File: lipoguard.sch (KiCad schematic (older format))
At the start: 13 parts, among them P1 CONN_2, P2 CONN_2, Q1 BC 850C, U1 BTS6143

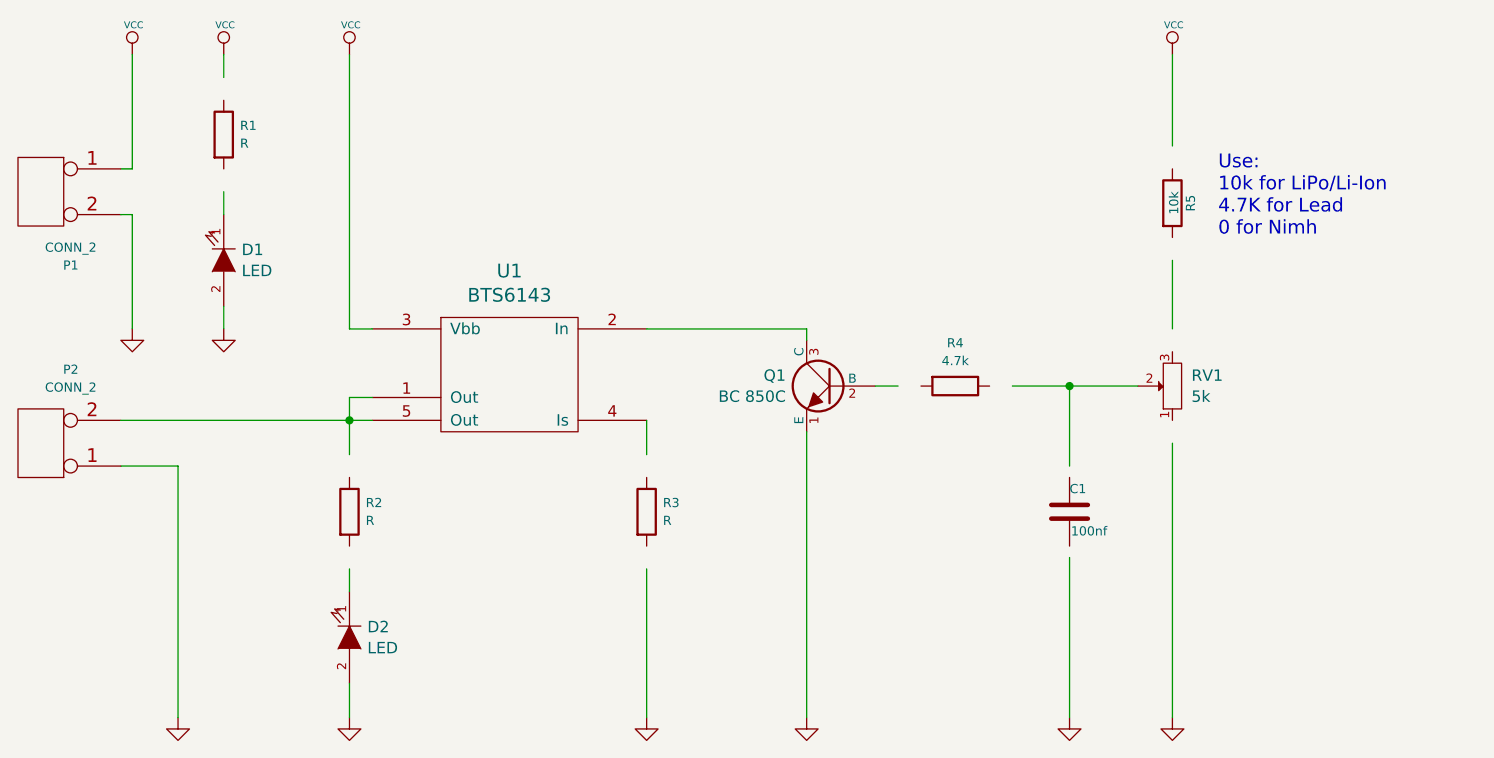
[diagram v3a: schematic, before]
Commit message: Updated symbols to new kicad libraries Added missing values Updated pdfs
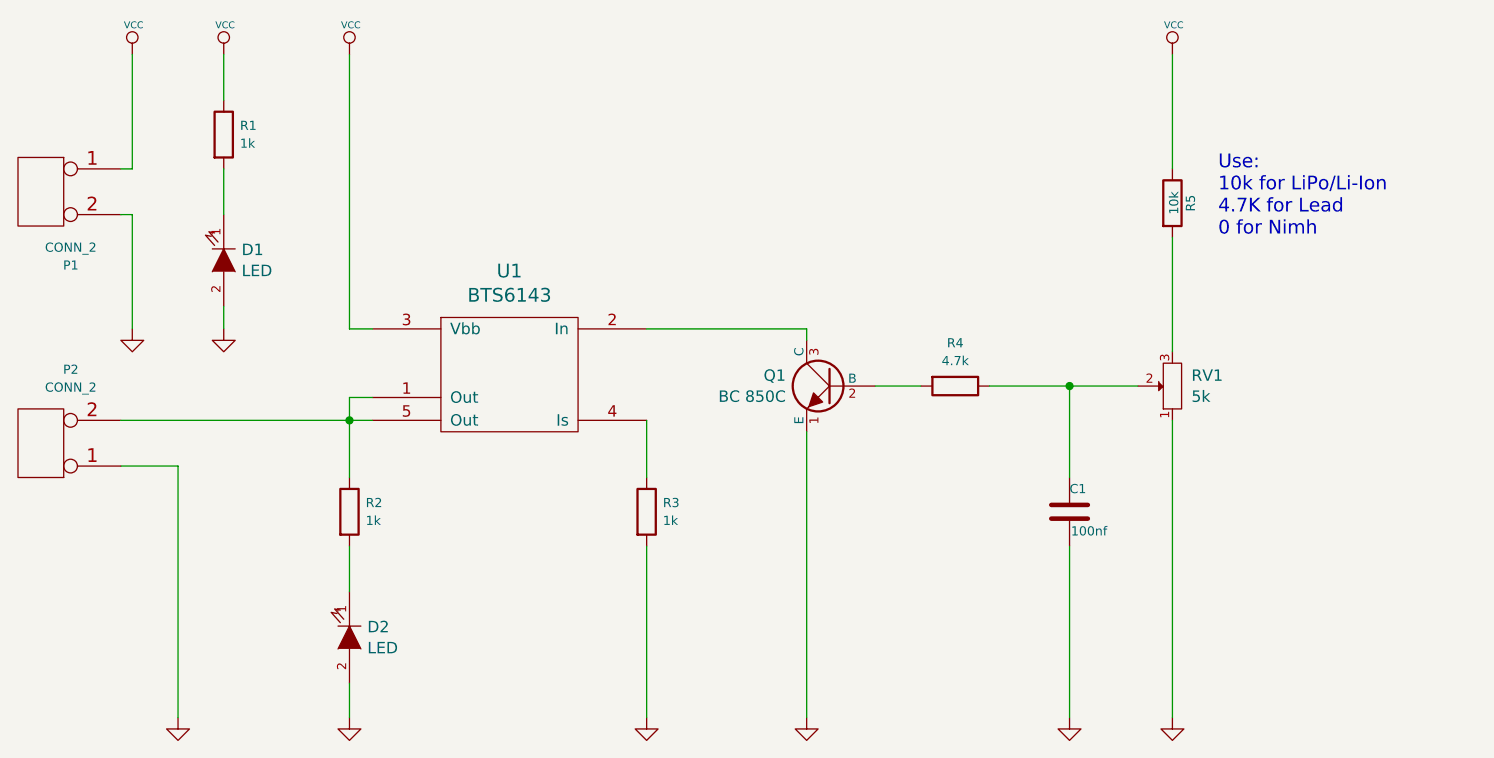
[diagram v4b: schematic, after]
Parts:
- R1, R2, R3: value R -> 1k
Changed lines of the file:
@@
 EESchema Schematic File Version 2
+LIBS:lipoguard-rescue
 LIBS:power
 LIBS:device
@@
 P 5900 4450
 F 0 "R3" H 5971 4489 40  0000 L CNN
-F 1 "R" H 5971 4411 40  0000 L CNN
+F 1 "1k" H 5971 4411 40  0000 L CNN
 F 2 "libcms:SM0603" V 5830 4450 30  0001 C CNN
 F 3 "" H 5900 4450 30  0000 C CNN
@@
 	1    0    0    -1
 $EndComp
-Wire Wire Line
-	5900 4050 5900 4200
-Wire Wire Line
-	5900 5350 5900 4700
-Wire Wire Line
-	4700 3650 4600 3650
-Wire Wire Line
-	4600 3650 4600 2450
 $Comp
 L VCC #PWR02
@@
 	-1   0    0    1
 $EndComp
-Wire Wire Line
-	4700 3950 4600 3950
-Wire Wire Line
-	4600 3950 4600 4200
-Wire Wire Line
-	3600 4050 4700 4050
-Wire Wire Line
-	3600 4250 3850 4250
-Wire Wire Line
-	3850 4250 3850 5350
 $Comp
 L GND #PWR03
@@
 	1    0    0    -1
 $EndComp
-Connection ~ 4600 4050
 $Comp
 L R R2
@@
 P 4600 4450
 F 0 "R2" H 4671 4489 40  0000 L CNN
-F 1 "R" H 4671 4411 40  0000 L CNN
+F 1 "1k" H 4671 4411 40  0000 L CNN
 F 2 "libcms:SM0603" V 4530 4450 30  0001 C CNN
 F 3 "" H 4600 4450 30  0000 C CNN
@@
 	0    1    1    0
 $EndComp
-Wire Wire Line
-	4600 4700 4600 4800
 $Comp
 L GND #PWR04
@@
 	1    0    0    -1
 $EndComp
-Wire Wire Line
-	4600 5350 4600 5200
 $Comp
 L VCC #PWR05
@@
 P 4050 2800
 F 0 "R1" H 4121 2839 40  0000 L CNN
-F 1 "R" H 4121 2761 40  0000 L CNN
+F 1 "1k" H 4121 2761 40  0000 L CNN
 F 2 "libcms:SM0603" V 3980 2800 30  0001 C CNN
 F 3 "" H 4050 2800 30  0000 C CNN
@@
 	1    0    0    -1
 $EndComp
-Wire Wire Line
-	4050 2450 4050 2550
-Wire Wire Line
-	4050 3050 4050 3150
-Wire Wire Line
-	4050 3650 4050 3550
 $Comp
 L CONN_2 P1
@@
 	-1   0    0    -1
 $EndComp
-Wire Wire Line
-	3600 2950 3650 2950
-Wire Wire Line
-	3650 2950 3650 2450
-Wire Wire Line
-	3600 3150 3650 3150
-Wire Wire Line
-	3650 3150 3650 3650
 $Comp
 L GND #PWR07
@@
 	-1   0    0    -1
 $EndComp
-Wire Wire Line
-	6600 3650 6600 3700
-Wire Wire Line
-	5900 3650 6600 3650
-Wire Wire Line
-	6600 4100 6600 5350
 $Comp
 L GND #PWR09
@@
 	0    1    1    0
 $EndComp
-Wire Wire Line
-	6900 3900 7000 3900
-Wire Wire Line
-	7500 3900 8050 3900
-Wire Wire Line
-	8200 4150 8200 5350
 $Comp
 L GND #PWR010
@@
 	1    0    0    -1
 $EndComp
-Wire Wire Line
-	7750 4250 7750 3900
-Connection ~ 7750 3900
-Wire Wire Line
-	7750 4650 7750 5350
 $Comp
 L GND #PWR012
@@
 	1    0    0    -1
 $EndComp
-Wire Wire Line
-	8200 3650 8200 3350
-Wire Wire Line
-	8200 2850 8200 2450
 Text Notes 8400 3250 0    60   ~ 0
 Use:\n10k for LiPo/Li-Ion\n4.7K for Lead\n0 for Nimh
+Wire Wire Line
+	5900 4050 5900 4300
+Wire Wire Line
+	5900 4600 5900 5350
+Wire Wire Line
+	4700 3650 4600 3650
+Wire Wire Line
+	4600 3650 4600 2450
+Wire Wire Line
+	4700 3950 4600 3950
+Wire Wire Line
+	4600 3950 4600 4300
+Wire Wire Line
+	3600 4050 4700 4050
+Wire Wire Line
+	3600 4250 3850 4250
+Wire Wire Line
+	3850 4250 3850 5350
+Connection ~ 4600 4050
+Wire Wire Line
+	4600 4600 4600 4800
+Wire Wire Line
+	4600 5350 4600 5200
+Wire Wire Line
+	4050 2450 4050 2650
+Wire Wire Line
+	4050 2950 4050 3150
+Wire Wire Line
+	4050 3650 4050 3550
+Wire Wire Line
+	3600 2950 3650 2950
+Wire Wire Line
+	3650 2950 3650 2450
+Wire Wire Line
+	3600 3150 3650 3150
+Wire Wire Line
+	3650 3150 3650 3650
+Wire Wire Line
+	6600 3650 6600 3700
+Wire Wire Line
+	5900 3650 6600 3650
+Wire Wire Line
+	6600 4100 6600 5350
+Wire Wire Line
+	6900 3900 7100 3900
+Wire Wire Line
+	7400 3900 8050 3900
+Wire Wire Line
+	8200 4050 8200 5350
+Wire Wire Line
+	7750 3900 7750 4300
+Connection ~ 7750 3900
+Wire Wire Line
+	7750 4600 7750 5350
+Wire Wire Line
+	8200 3250 8200 3750
+Wire Wire Line
+	8200 2450 8200 2950
 $EndSCHEMATC
